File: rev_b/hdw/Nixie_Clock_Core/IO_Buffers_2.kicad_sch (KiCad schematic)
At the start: 14 parts

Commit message: lots of core board routing
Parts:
- removed R?: 10K, Resistors_SMD:R_0603, symbol Custom_Library:R_Custom
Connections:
- net Pushbutton_0: now also RN?.16 (R1.2); no longer R?.2
- net Pushbutton_0_DSP: now also RN?.9 (R8.2)
- net ~{Display_Detect_DSP}: no longer RN?.16 (R1.2)
- net ~{Display_Detect}: now also R?.2; no longer RN?.9 (R8.2)
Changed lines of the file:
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@@
   (junction (at 80.01 146.05) (diameter 0) (color 0 0 0 0)
   )
+  (junction (at 92.71 106.68) (diameter 0) (color 0 0 0 0)
+  )
   (junction (at 171.45 146.05) (diameter 0) (color 0 0 0 0)
   )
   (junction (at 168.91 121.92) (diameter 0) (color 0 0 0 0)
   )
-  (junction (at 184.15 106.68) (diameter 0) (color 0 0 0 0)
+  (junction (at 92.71 124.46) (diameter 0) (color 0 0 0 0)
   )
   (junction (at 87.63 119.38) (diameter 0) (color 0 0 0 0)
@@
   (junction (at 181.61 109.22) (diameter 0) (color 0 0 0 0)
   )
+  (junction (at 166.37 124.46) (diameter 0) (color 0 0 0 0)
+  )
   (junction (at 160.02 63.5) (diameter 0) (color 0 0 0 0)
   )
-  (junction (at 92.71 124.46) (diameter 0) (color 0 0 0 0)
-  )
   (junction (at 181.61 146.05) (diameter 0) (color 0 0 0 0)
   )
@@
   (junction (at 173.99 146.05) (diameter 0) (color 0 0 0 0)
   )
-  (junction (at 166.37 124.46) (diameter 0) (color 0 0 0 0)
-  )
   (junction (at 85.09 116.84) (diameter 0) (color 0 0 0 0)
   )
@@
   (junction (at 173.99 116.84) (diameter 0) (color 0 0 0 0)
   )
-  (junction (at 74.93 106.68) (diameter 0) (color 0 0 0 0)
-  )
   (junction (at 77.47 146.05) (diameter 0) (color 0 0 0 0)
   )
+  (junction (at 166.37 106.68) (diameter 0) (color 0 0 0 0)
+  )
   (junction (at 90.17 146.05) (diameter 0) (color 0 0 0 0)
   )
@@
   (junction (at 82.55 114.3) (diameter 0) (color 0 0 0 0)
   )
-  (no_connect (at 92.71 134.62))
-  (no_connect (at 166.37 134.62))
+  (no_connect (at 184.15 134.62))
+  (no_connect (at 74.93 134.62))
   (wire (pts (xy 116.84 119.38) (xy 87.63 119.38))
     (stroke (width 0) (type default))
@@
     (stroke (width 0) (type default))
   )
-  (wire (pts (xy 92.71 124.46) (xy 64.77 124.46))
-    (stroke (width 0) (type default))
-  )
-  (wire (pts (xy 74.93 134.62) (xy 74.93 106.68))
+  (wire (pts (xy 64.77 124.46) (xy 92.71 124.46))
     (stroke (width 0) (type default))
   )
@@
     (stroke (width 0) (type default))
   )
+  (wire (pts (xy 92.71 124.46) (xy 92.71 134.62))
+    (stroke (width 0) (type default))
+  )
   (wire (pts (xy 143.51 129.54) (xy 194.31 129.54))
     (stroke (width 0) (type default))
@@
     (stroke (width 0) (type default))
   )
-  (wire (pts (xy 166.37 100.33) (xy 166.37 124.46))
-    (stroke (width 0) (type default))
-  )
   (wire (pts (xy 142.24 132.08) (xy 143.51 132.08))
     (stroke (width 0) (type default))
   )
-  (wire (pts (xy 116.84 106.68) (xy 74.93 106.68))
+  (wire (pts (xy 166.37 100.33) (xy 166.37 106.68))
     (stroke (width 0) (type default))
   )
@@
     (stroke (width 0) (type default))
   )
-  (wire (pts (xy 142.24 106.68) (xy 184.15 106.68))
+  (wire (pts (xy 92.71 100.33) (xy 92.71 106.68))
     (stroke (width 0) (type default))
   )
@@
     (stroke (width 0) (type default))
   )
+  (wire (pts (xy 166.37 124.46) (xy 194.31 124.46))
+    (stroke (width 0) (type default))
+  )
   (wire (pts (xy 179.07 144.78) (xy 179.07 146.05))
     (stroke (width 0) (type default))
@@
     (stroke (width 0) (type default))
   )
-  (wire (pts (xy 64.77 106.68) (xy 74.93 106.68))
+  (wire (pts (xy 64.77 106.68) (xy 92.71 106.68))
     (stroke (width 0) (type default))
   )
@@
     (stroke (width 0) (type default))
   )
-  (wire (pts (xy 92.71 124.46) (xy 92.71 100.33))
-    (stroke (width 0) (type default))
-  )
   (wire (pts (xy 176.53 144.78) (xy 176.53 146.05))
     (stroke (width 0) (type default))
@@
     (stroke (width 0) (type default))
   )
+  (wire (pts (xy 92.71 124.46) (xy 116.84 124.46))
+    (stroke (width 0) (type default))
+  )
   (wire (pts (xy 168.91 134.62) (xy 168.91 121.92))
     (stroke (width 0) (type default))
@@
     (stroke (width 0) (type default))
   )
-  (wire (pts (xy 184.15 134.62) (xy 184.15 106.68))
-    (stroke (width 0) (type default))
-  )
   (wire (pts (xy 168.91 121.92) (xy 194.31 121.92))
     (stroke (width 0) (type default))
@@
     (stroke (width 0) (type default))
   )
-  (wire (pts (xy 116.84 124.46) (xy 92.71 124.46))
-    (stroke (width 0) (type default))
-  )
   (wire (pts (xy 166.37 146.05) (xy 166.37 144.78))
     (stroke (width 0) (type default))
@@
     (stroke (width 0) (type default))
   )
-  (wire (pts (xy 166.37 124.46) (xy 194.31 124.46))
-    (stroke (width 0) (type default))
-  )
   (wire (pts (xy 142.24 109.22) (xy 181.61 109.22))
     (stroke (width 0) (type default))
@@
     (stroke (width 0) (type default))
   )
-  (wire (pts (xy 194.31 106.68) (xy 184.15 106.68))
+  (wire (pts (xy 142.24 106.68) (xy 166.37 106.68))
     (stroke (width 0) (type default))
   )
@@
     (stroke (width 0) (type default))
   )
+  (wire (pts (xy 92.71 106.68) (xy 116.84 106.68))
+    (stroke (width 0) (type default))
+  )
   (wire (pts (xy 64.77 114.3) (xy 82.55 114.3))
     (stroke (width 0) (type default))
@@
     (stroke (width 0) (type default))
   )
+  (wire (pts (xy 166.37 124.46) (xy 166.37 134.62))
+    (stroke (width 0) (type default))
+  )
   (wire (pts (xy 87.63 146.05) (xy 85.09 146.05))
     (stroke (width 0) (type default))
   )
   (wire (pts (xy 171.45 146.05) (xy 173.99 146.05))
+    (stroke (width 0) (type default))
+  )
+  (wire (pts (xy 166.37 106.68) (xy 194.31 106.68))
     (stroke (width 0) (type default))
   )
@@
         )
       )
-    )
-  )
-  (symbol (lib_id "Custom_Library:R_Custom") (at 166.37 96.52 0) (mirror y) (unit 1)
-    (in_bom yes) (on_board yes) (dnp no)
-    (property "Reference" "R?" (at 167.894 96.52 0)
-      (effects (font (size 1.27 1.27)) (justify right))
-    )
-    (property "Value" "10K" (at 166.37 96.52 90)
-      (effects (font (size 1.27 1.27)))
-    )
-    (property "Footprint" "Resistors_SMD:R_0603" (at 166.37 96.52 0)
-      (effects (font (size 1.27 1.27)) hide)
-    )
-    (property "Datasheet" "" (at 166.37 96.52 0)
-      (effects (font (size 1.27 1.27)) hide)
-    )
-    (property "display_footprint" "0603" (at 164.592 94.234 0)
-      (effects (font (size 1.27 1.27)) (justify left) hide)
-    )
-    (property "Tolerance" "1%" (at 164.592 96.52 0)
-      (effects (font (size 1.27 1.27)) (justify left) hide)
-    )
-    (property "Wattage" "1/10W" (at 164.592 98.552 0)
-      (effects (font (size 1.27 1.27)) (justify left) hide)
-    )
-    (property "Digi-Key PN" "" (at 158.75 86.36 0)
-      (effects (font (size 1.524 1.524)) hide)
-    )
-    (pin "1")
-    (pin "2")
-    (instances
-      (project "VFD_Clock"
-        (path "/0e0fa043-3ab8-4cb9-8105-f968ef03a597/00000000-0000-0000-0000-00005bb6cf6d"
-          (reference "R?") (unit 1)
-        )
-        (path "/0e0fa043-3ab8-4cb9-8105-f968ef03a597/00000000-0000-0000-0000-00005cb8a16a"
-          (reference "R?") (unit 1)
-        )
-        (path "/0e0fa043-3ab8-4cb9-8105-f968ef03a597/00000000-0000-0000-0000-00005baae2b6"
-          (reference "R?") (unit 1)
-        )
-        (path "/0e0fa043-3ab8-4cb9-8105-f968ef03a597/00000000-0000-0000-0000-00005cc31b3e"
-          (reference "R?") (unit 1)
-        )
-        (path "/0e0fa043-3ab8-4cb9-8105-f968ef03a597/00000000-0000-0000-0000-00005bbe424c"
-          (reference "R?") (unit 1)
-        )
-      )
-      (project "Nixie_Clock_Core"
-        (path "/16fdce21-b570-4d81-a458-e8839d611806/8bfc37a9-2570-4706-99e7-147636a5a42e"
-          (reference "R1806") (unit 1)
-        )
-      )

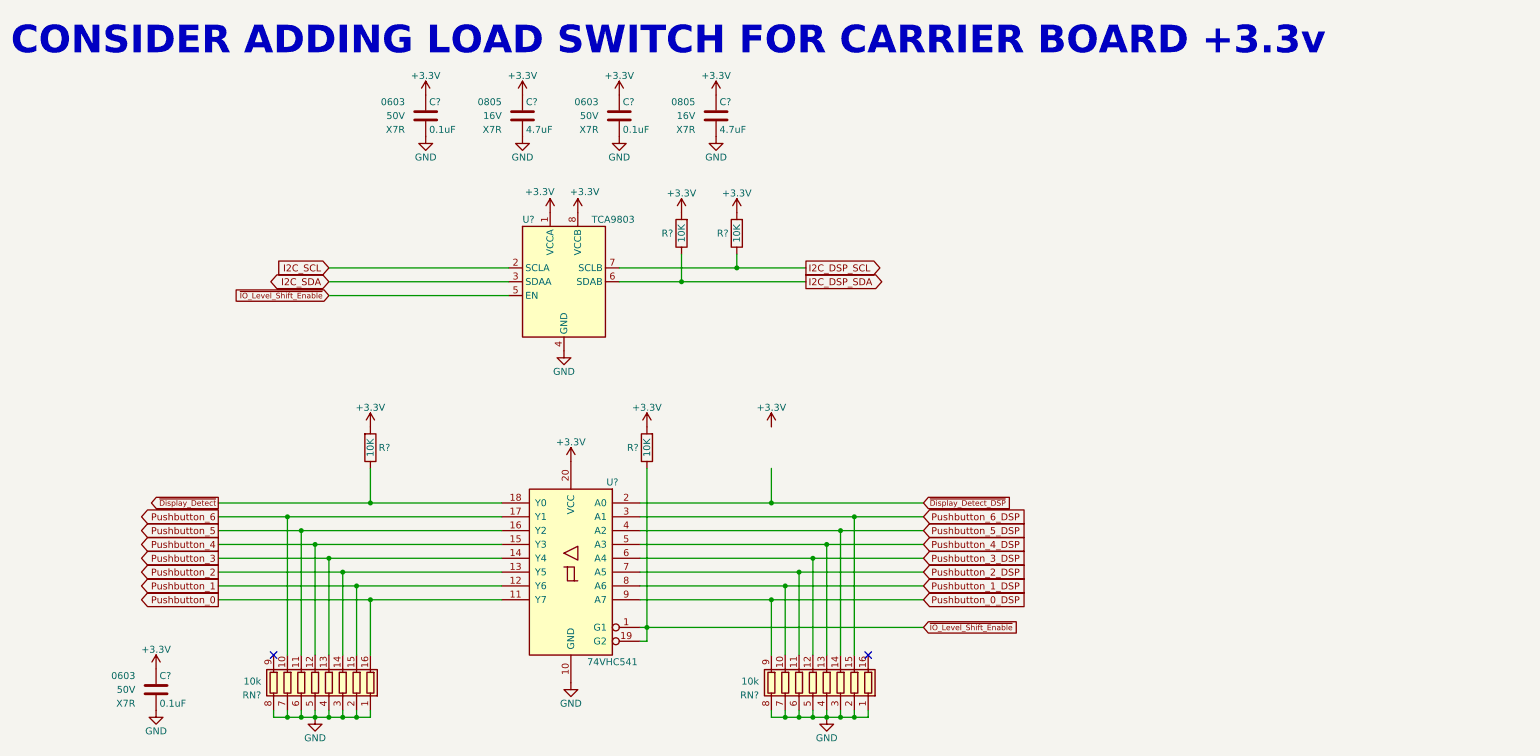
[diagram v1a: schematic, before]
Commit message: added BOM
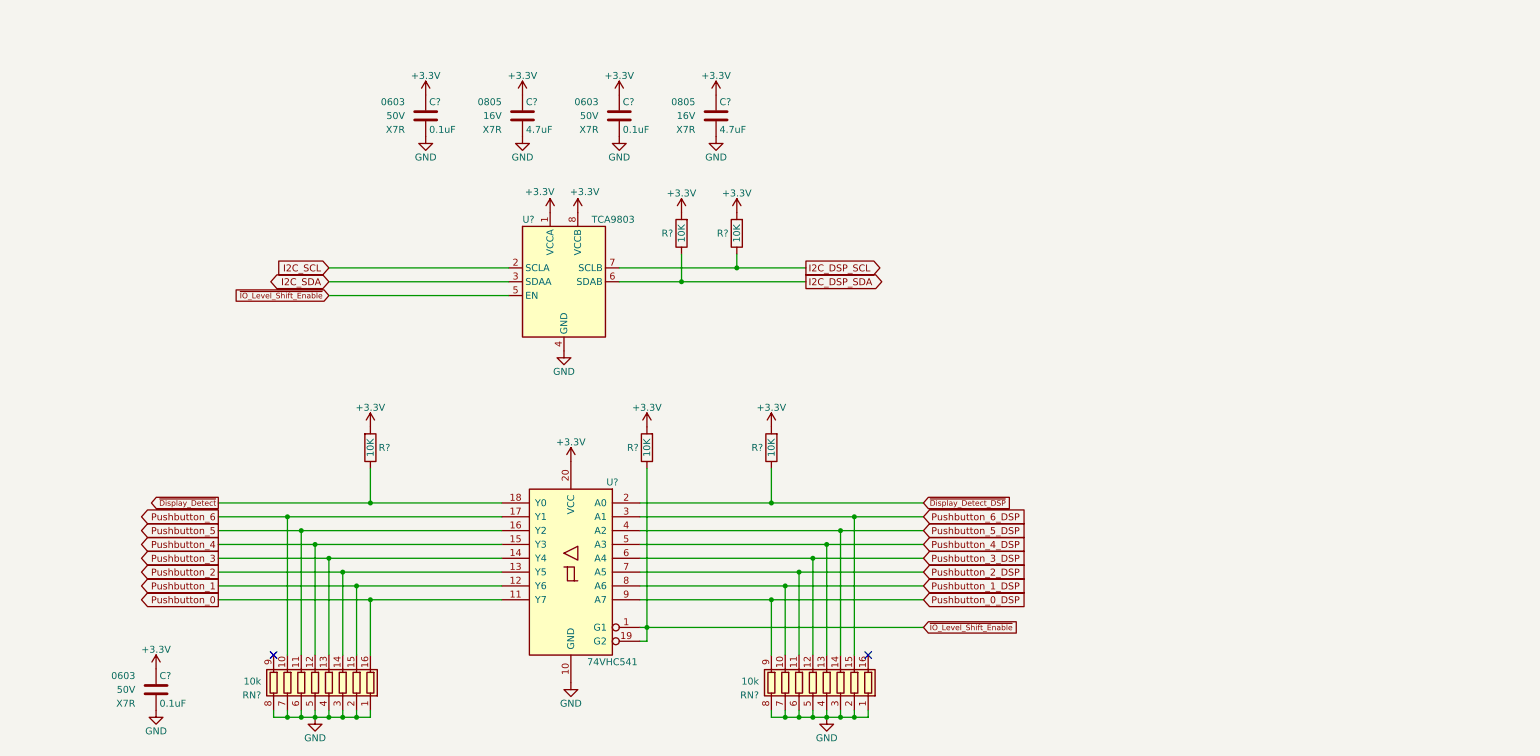
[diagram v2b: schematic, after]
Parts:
- added R?: 10K, Resistors_SMD:R_0603, symbol Custom_Library:R_Custom
- R? (x4): Digi-Key PN (none) -> 541-10.0KHCT-ND
- RN? (x2): Tolerance (none) -> 1%
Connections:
- net +3.3V: now also R?.1
- net ~{Display_Detect_DSP}: now also R?.2
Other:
- note removed: "CONSIDER ADDING LOAD SWITCH FOR CARRIER BOARD +3.3v"
- title: (none) -> Nixie Clock Redux Core Board
